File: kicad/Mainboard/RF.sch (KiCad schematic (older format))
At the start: 110 parts, among them J8 Antenna, Q3 BGA6589, T1 AFT05MS004NT1, U13 BGA2874, U5 ADF7021, U6 HMC546MS8GETR, U7 LM2904A, X1 12.288MHz

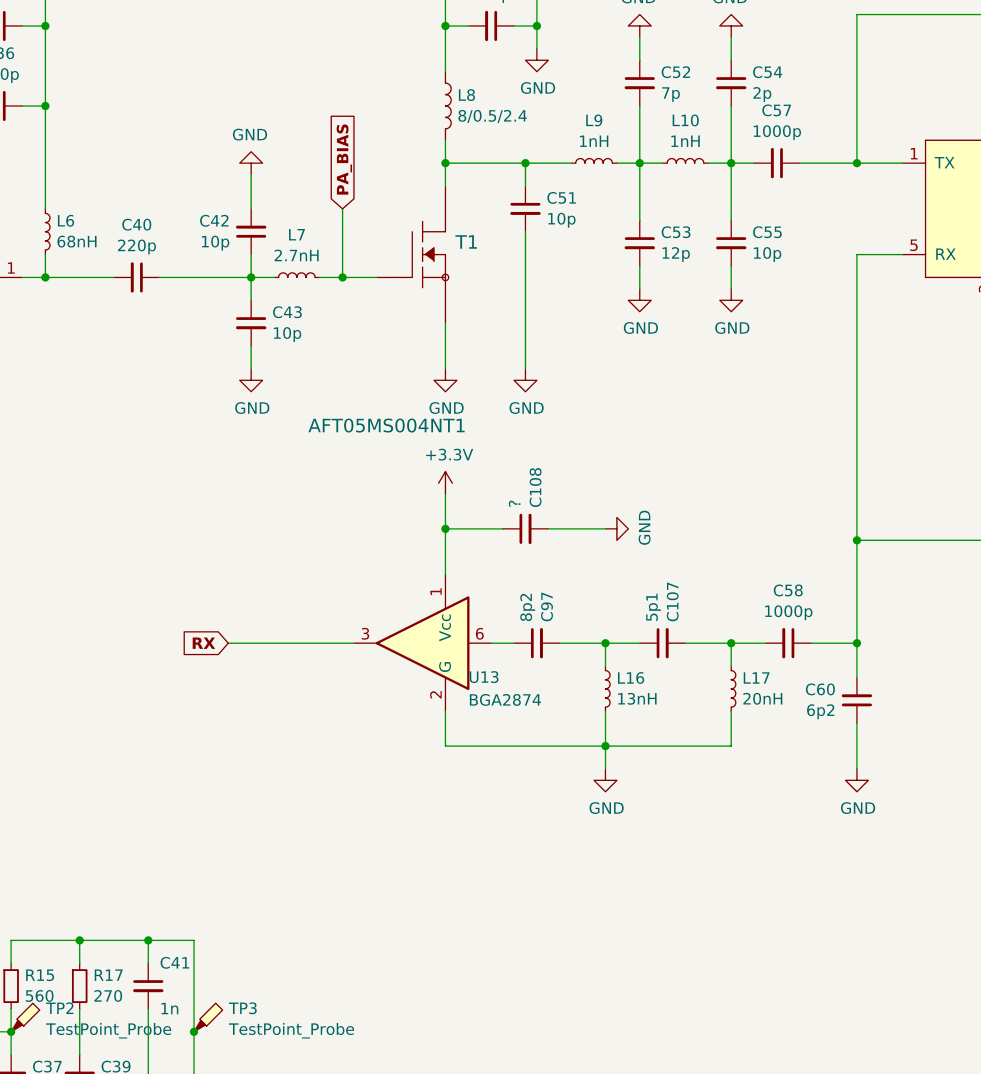
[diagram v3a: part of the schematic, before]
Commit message: added RF switch on-off transistor, plotted new schematic
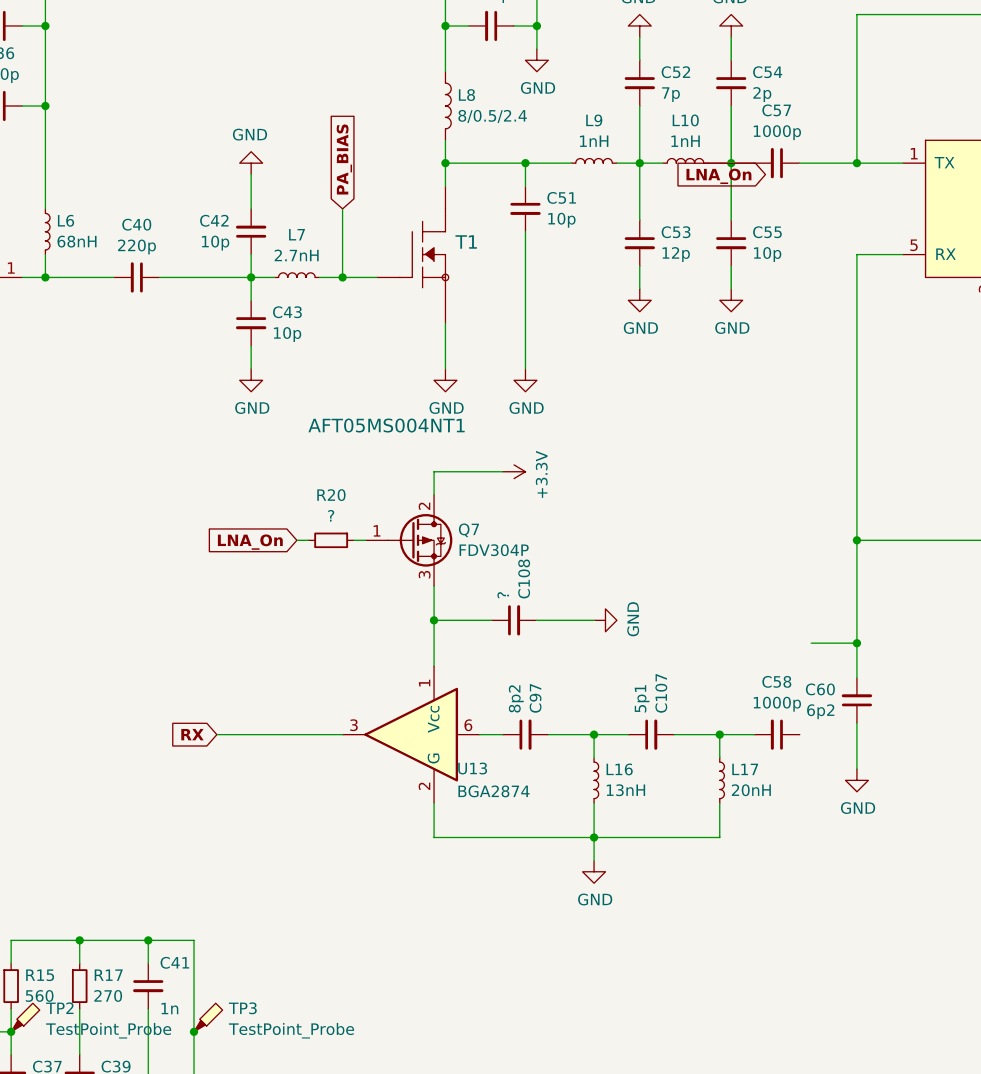
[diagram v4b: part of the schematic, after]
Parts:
- added Q7: FDV304P, Package_TO_SOT_SMD:SOT-23, symbol Device:Q_PMOS_GDS
- added R20: ?, Resistor_SMD:R_0603_1608Metric, symbol Mainboard-rescue:R_Small-Device
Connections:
- net +3V3: now also Q7.2 (D); no longer C108.1, U13.1 (Vcc)
- net at C60.2, L12.1, U6.5 (RX): no longer C58.1
- new net: C108.1, Q7.3 (S), U13.1 (Vcc)
- new net: Q7.1 (G), R20.1
- new net LNA_On: R20.2
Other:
- moved on the sheet: C107, C108, C58, C97, L16, L17, U13
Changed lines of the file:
@@
 L Mainboard-rescue:C_Small-device C58
 U 1 1 5DF79664
-P 7850 4600
-F 0 "C58" V 7621 4600 50  0000 C CNN
-F 1 "1000p" V 7712 4600 50  0000 C CNN
-F 2 "Capacitor_SMD:C_0603_1608Metric" H 7850 4600 50  0001 C CNN
-F 3 "~" H 7850 4600 50  0001 C CNN
-	1    7850 4600
+P 7800 5000
+F 0 "C58" V 7571 5000 50  0000 C CNN
+F 1 "1000p" V 7662 5000 50  0000 C CNN
+F 2 "Capacitor_SMD:C_0603_1608Metric" H 7800 5000 50  0001 C CNN
+F 3 "~" H 7800 5000 50  0001 C CNN
+	1    7800 5000
 	0    1    1    0
 $EndComp
@@
 Wire Wire Line
 	8150 2900 8150 4150
-Text GLabel 5400 4600 0    50   Input ~ 10
+Text GLabel 5350 5000 0    50   Input ~ 10
 RX
 Text GLabel 14950 4000 2    50   Input ~ 10
@@
 L RF_Amplifier:BGA2874 U13
 U 1 1 5EB02D36
-P 6250 4600
-F 0 "U13" H 6050 4450 50  0000 R CNN
-F 1 "BGA2874" H 6050 4350 50  0000 R CNN
-F 2 "Package_TO_SOT_SMD:SOT-363_SC-70-6" H 6200 3950 50  0001 C CNN
-F 3 "https://www.nxp.com/docs/en/data-sheet/BGA2874.pdf" H 6250 4600 50  0001 C CNN
-	1    6250 4600
+P 6200 5000
+F 0 "U13" H 6000 4850 50  0000 R CNN
+F 1 "BGA2874" H 6000 4750 50  0000 R CNN
+F 2 "Package_TO_SOT_SMD:SOT-363_SC-70-6" H 6150 4350 50  0001 C CNN
+F 3 "https://www.nxp.com/docs/en/data-sheet/BGA2874.pdf" H 6200 5000 50  0001 C CNN
+	1    6200 5000
 	-1   0    0    -1
 $EndComp
@@
 L Device:L_Small L17
 U 1 1 5EB6932C
-P 7600 4800
-F 0 "L17" H 7648 4846 50  0000 L CNN
-F 1 "20nH" H 7648 4755 50  0000 L CNN
-F 2 "Inductor_SMD:L_0603_1608Metric" H 7600 4800 50  0001 C CNN
-F 3 "~" H 7600 4800 50  0001 C CNN
-	1    7600 4800
+P 7550 5200
+F 0 "L17" H 7598 5246 50  0000 L CNN
+F 1 "20nH" H 7598 5155 50  0000 L CNN
+F 2 "Inductor_SMD:L_0603_1608Metric" H 7550 5200 50  0001 C CNN
+F 3 "~" H 7550 5200 50  0001 C CNN
+	1    7550 5200
 	1    0    0    -1
 $EndComp
@@
 L Mainboard-rescue:C_Small-Device C107
 U 1 1 5EB6AF5F
-P 7300 4600
-F 0 "C107" H 7208 4554 50  0000 R CNN
-F 1 "5p1" H 7208 4645 50  0000 R CNN
-F 2 "Capacitor_SMD:C_0603_1608Metric" H 7300 4600 50  0001 C CNN
-F 3 "~" H 7300 4600 50  0001 C CNN
-	1    7300 4600
+P 7250 5000
+F 0 "C107" H 7158 4954 50  0000 R CNN
+F 1 "5p1" H 7158 5045 50  0000 R CNN
+F 2 "Capacitor_SMD:C_0603_1608Metric" H 7250 5000 50  0001 C CNN
+F 3 "~" H 7250 5000 50  0001 C CNN
+	1    7250 5000
 	0    -1   1    0
 $EndComp
@@
 L Device:L_Small L16
 U 1 1 5EB6CEAB
-P 7050 4800
-F 0 "L16" H 7098 4846 50  0000 L CNN
-F 1 "13nH" H 7098 4755 50  0000 L CNN
-F 2 "Inductor_SMD:L_0603_1608Metric" H 7050 4800 50  0001 C CNN
-F 3 "~" H 7050 4800 50  0001 C CNN
-	1    7050 4800
+P 7000 5200
+F 0 "L16" H 7048 5246 50  0000 L CNN
+F 1 "13nH" H 7048 5155 50  0000 L CNN
+F 2 "Inductor_SMD:L_0603_1608Metric" H 7000 5200 50  0001 C CNN
+F 3 "~" H 7000 5200 50  0001 C CNN
+	1    7000 5200
 	1    0    0    -1
 $EndComp
@@
 L Mainboard-rescue:C_Small-Device C97
 U 1 1 5EB6D251
-P 6750 4600
-F 0 "C97" H 6658 4554 50  0000 R CNN
-F 1 "8p2" H 6658 4645 50  0000 R CNN
-F 2 "Capacitor_SMD:C_0603_1608Metric" H 6750 4600 50  0001 C CNN
-F 3 "~" H 6750 4600 50  0001 C CNN
-	1    6750 4600
+P 6700 5000
+F 0 "C97" H 6608 4954 50  0000 R CNN
+F 1 "8p2" H 6608 5045 50  0000 R CNN
+F 2 "Capacitor_SMD:C_0603_1608Metric" H 6700 5000 50  0001 C CNN
+F 3 "~" H 6700 5000 50  0001 C CNN
+	1    6700 5000
 	0    -1   1    0
 $EndComp
 Wire Wire Line
-	6550 4600 6650 4600
+	6500 5000 6600 5000
 $Comp
 L power:GND #PWR0120
 U 1 1 5EC16C67
-P 7050 5150
-F 0 "#PWR0120" H 7050 4900 50  0001 C CNN
-F 1 "GND" H 7055 4977 50  0000 C CNN
-F 2 "" H 7050 5150 50  0001 C CNN
-F 3 "" H 7050 5150 50  0001 C CNN
-	1    7050 5150
+P 7000 5550
+F 0 "#PWR0120" H 7000 5300 50  0001 C CNN
+F 1 "GND" H 7005 5377 50  0000 C CNN
+F 2 "" H 7000 5550 50  0001 C CNN
+F 3 "" H 7000 5550 50  0001 C CNN
+	1    7000 5550
 	1    0    0    -1
 $EndComp
@@
 L power:+3.3V #PWR0176
 U 1 1 5ECF6899
-P 6350 3950
-F 0 "#PWR0176" H 6350 3800 50  0001 C CNN
-F 1 "+3.3V" H 6365 4123 50  0000 C CNN
-F 2 "" H 6350 3950 50  0001 C CNN
-F 3 "" H 6350 3950 50  0001 C CNN
-	1    6350 3950
-	1    0    0    -1
+P 6600 3850
+F 0 "#PWR0176" H 6600 3700 50  0001 C CNN
+F 1 "+3.3V" H 6615 4023 50  0000 C CNN
+F 2 "" H 6600 3850 50  0001 C CNN
+F 3 "" H 6600 3850 50  0001 C CNN
+	1    6600 3850
+	0    1    1    0
 $EndComp
 $Comp
 L Mainboard-rescue:C_Small-Device C108
 U 1 1 5ED2084B
-P 6700 4100
-F 0 "C108" H 6608 4054 50  0000 R CNN
-F 1 "?" H 6608 4145 50  0000 R CNN
-F 2 "Capacitor_SMD:C_0603_1608Metric" H 6700 4100 50  0001 C CNN
-F 3 "~" H 6700 4100 50  0001 C CNN
-	1    6700 4100
+P 6650 4500
+F 0 "C108" H 6558 4454 50  0000 R CNN
+F 1 "?" H 6558 4545 50  0000 R CNN
+F 2 "Capacitor_SMD:C_0603_1608Metric" H 6650 4500 50  0001 C CNN
+F 3 "~" H 6650 4500 50  0001 C CNN
+	1    6650 4500
 	0    -1   1    0
 $EndComp
-Connection ~ 6350 4100
+Connection ~ 6300 4500
 $Comp
 L power:GND #PWR0177
 U 1 1 5ED3FE5B
-P 7050 4100
-F 0 "#PWR0177" H 7050 3850 50  0001 C CNN
-F 1 "GND" H 7055 3927 50  0000 C CNN
-F 2 "" H 7050 4100 50  0001 C CNN
-F 3 "" H 7050 4100 50  0001 C CNN
-	1    7050 4100
+P 7000 4500
+F 0 "#PWR0177" H 7000 4250 50  0001 C CNN
+F 1 "GND" H 7005 4327 50  0000 C CNN
+F 2 "" H 7000 4500 50  0001 C CNN
+F 3 "" H 7000 4500 50  0001 C CNN
+	1    7000 4500
 	0    -1   -1   0
 $EndComp
 Wire Wire Line
-	5400 4600 5950 4600
-Wire Wire Line
-	6800 4100 7050 4100
-Wire Wire Line
-	6350 4100 6600 4100
-Wire Wire Line
-	6350 3950 6350 4100
-Wire Wire Line
-	6350 4100 6350 4300
-Wire Wire Line
-	6850 4600 7050 4600
-Wire Wire Line
-	7050 4700 7050 4600
-Connection ~ 7050 4600
-Wire Wire Line
-	7050 4600 7200 4600
-Wire Wire Line
-	7400 4600 7600 4600
-Wire Wire Line
-	7600 4700 7600 4600
-Connection ~ 7600 4600
-Wire Wire Line
-	7600 4600 7750 4600
+	5350 5000 5900 5000
+Wire Wire Line
+	6750 4500 7000 4500
+Wire Wire Line
+	6300 4500 6550 4500
+Wire Wire Line
+	6300 4350 6300 4500
+Wire Wire Line
+	6300 4500 6300 4700
+Wire Wire Line
+	6800 5000 7000 5000
+Wire Wire Line
+	7000 5100 7000 5000
+Connection ~ 7000 5000
+Wire Wire Line
+	7000 5000 7150 5000
+Wire Wire Line
+	7350 5000 7550 5000
+Wire Wire Line
+	7550 5100 7550 5000
+Connection ~ 7550 5000
+Wire Wire Line
+	7550 5000 7700 5000
 Wire Wire Line
 	8150 4950 8150 5150
 Wire Wire Line
-	7600 4900 7600 5050
-Wire Wire Line
-	7600 5050 7050 5050
-Wire Wire Line
-	6350 5050 6350 4900
-Wire Wire Line
-	7050 4900 7050 5050
-Connection ~ 7050 5050
-Wire Wire Line
-	7050 5050 6350 5050
-Wire Wire Line
-	7050 5050 7050 5150
+	7550 5300 7550 5450
+Wire Wire Line
+	7550 5450 7000 5450
+Wire Wire Line
+	6300 5450 6300 5300
+Wire Wire Line
+	7000 5300 7000 5450
+Connection ~ 7000 5450
+Wire Wire Line
+	7000 5450 6300 5450
+Wire Wire Line
+	7000 5450 7000 5550
+Wire Wire Line
+	6300 3850 6300 3950
+Wire Wire Line
+	6300 3850 6600 3850
+$Comp
+L Mainboard-rescue:R_Small-Device R20
+U 1 1 5ECF3BC5
+P 5850 4150
+F 0 "R20" V 5654 4150 50  0000 C CNN
+F 1 "?" V 5745 4150 50  0000 C CNN
+F 2 "Resistor_SMD:R_0603_1608Metric" H 5850 4150 50  0001 C CNN
+F 3 "~" H 5850 4150 50  0001 C CNN
+	1    5850 4150
+	0    1    1    0
+$EndComp
+Wire Wire Line
+	5950 4150 6000 4150
+Wire Wire Line
+	5750 4150 5700 4150
+$Comp
+L Device:Q_PMOS_GDS Q7
+U 1 1 5ED3A378
+P 6200 4150
+F 0 "Q7" H 6405 4196 50  0000 L CNN
+F 1 "FDV304P" H 6405 4105 50  0000 L CNN
+F 2 "Package_TO_SOT_SMD:SOT-23" H 6400 4250 50  0001 C CNN
+F 3 "~" H 6200 4150 50  0001 C CNN
+	1    6200 4150
+	1    0    0    -1
+$EndComp
+Text GLabel 5700 4150 0    50   Input ~ 10
+LNA_On
+Text GLabel 7750 2550 0    50   Input ~ 10
+LNA_On
 $EndSCHEMATC

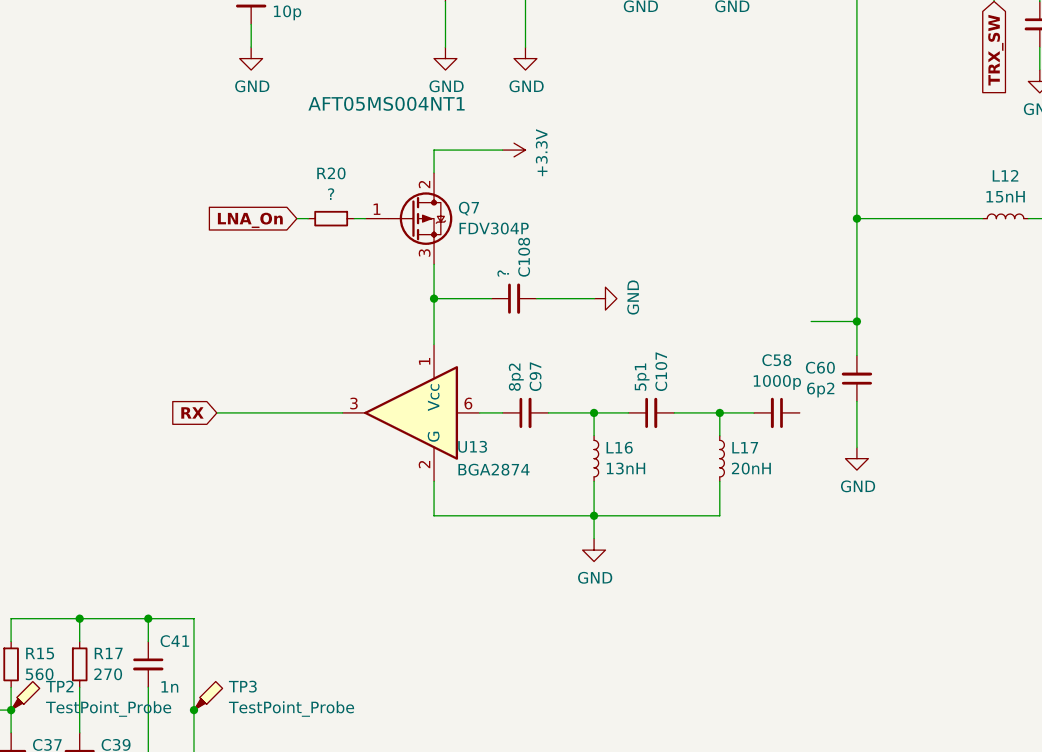
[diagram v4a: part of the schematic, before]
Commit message: fixed p-mos alignment :)
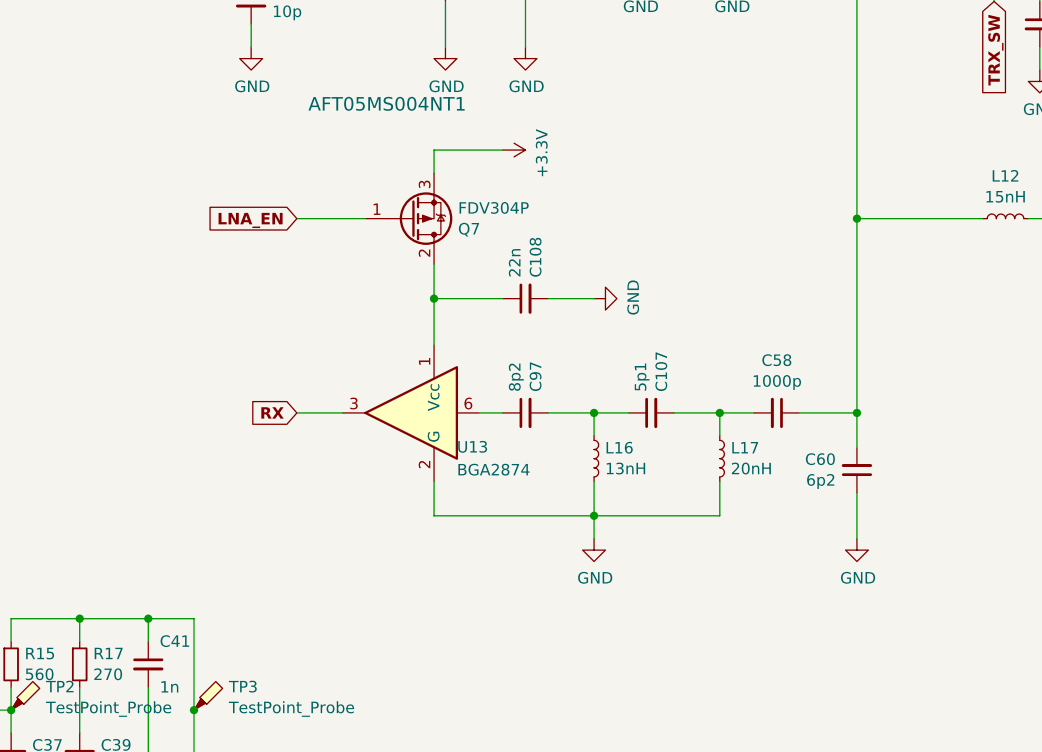
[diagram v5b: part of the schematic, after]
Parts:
- removed R20: ?, Resistor_SMD:R_0603_1608Metric, symbol Mainboard-rescue:R_Small-Device
- C108: value ? -> 22n
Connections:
- net +3V3: now also Q7.3 (S); no longer Q7.2 (D)
- net at C60.2, L12.1, U6.5 (RX): now also C58.1
- net at C108.1, U13.1 (Vcc): now also Q7.2 (D); no longer Q7.3 (S)
- net LNA_EN: now reaches Q7.1 (G)
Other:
- moved on the sheet: C108, C60
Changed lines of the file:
@@
 EESchema Schematic File Version 4
+LIBS:Mainboard-cache
 EELAYER 30 0
 EELAYER END
@@
 Wire Wire Line
 	8150 2900 8150 4150
-Text GLabel 5350 5000 0    50   Input ~ 10
+Text GLabel 5700 5000 0    50   Input ~ 10
 RX
 Text GLabel 14950 4000 2    50   Input ~ 10
@@
 	0    -1   -1   0
 $EndComp
-Connection ~ 8150 4150
 Wire Wire Line
 	9750 4150 9750 2700
@@
 L Mainboard-rescue:C_Small-Device C60
 U 1 1 5E09CAD6
-P 8150 4850
-F 0 "C60" H 8058 4804 50  0000 R CNN
-F 1 "6p2" H 8058 4895 50  0000 R CNN
-F 2 "Capacitor_SMD:C_0603_1608Metric" H 8150 4850 50  0001 C CNN
-F 3 "~" H 8150 4850 50  0001 C CNN
-	1    8150 4850
+P 8150 5250
+F 0 "C60" H 8058 5204 50  0000 R CNN
+F 1 "6p2" H 8058 5295 50  0000 R CNN
+F 2 "Capacitor_SMD:C_0603_1608Metric" H 8150 5250 50  0001 C CNN
+F 3 "~" H 8150 5250 50  0001 C CNN
+	1    8150 5250
 	1    0    0    1
 $EndComp
@@
 L power:GND #PWR098
 U 1 1 5E0A2231
-P 8150 5150
-F 0 "#PWR098" H 8150 4900 50  0001 C CNN
-F 1 "GND" H 8155 4977 50  0000 C CNN
-F 2 "" H 8150 5150 50  0001 C CNN
-F 3 "" H 8150 5150 50  0001 C CNN
-	1    8150 5150
-	1    0    0    -1
-$EndComp
-Wire Wire Line
-	8150 4150 8150 4600
+P 8150 5550
+F 0 "#PWR098" H 8150 5300 50  0001 C CNN
+F 1 "GND" H 8155 5377 50  0000 C CNN
+F 2 "" H 8150 5550 50  0001 C CNN
+F 3 "" H 8150 5550 50  0001 C CNN
+	1    8150 5550
+	1    0    0    -1
+$EndComp
 $Comp
 L Mainboard-rescue:C_Small-Device C62
@@
 	1    0    0    -1
 $EndComp
-Wire Wire Line
-	7950 4600 8150 4600
-Connection ~ 8150 4600
-Wire Wire Line
-	8150 4600 8150 4750
+Connection ~ 8150 5000
+Wire Wire Line
+	8150 5000 8150 5150
 $Comp
 L power:+3.3V #PWR0176
@@
 L Mainboard-rescue:C_Small-Device C108
 U 1 1 5ED2084B
-P 6650 4500
-F 0 "C108" H 6558 4454 50  0000 R CNN
-F 1 "?" H 6558 4545 50  0000 R CNN
-F 2 "Capacitor_SMD:C_0603_1608Metric" H 6650 4500 50  0001 C CNN
-F 3 "~" H 6650 4500 50  0001 C CNN
-	1    6650 4500
+P 6700 4500
+F 0 "C108" H 6608 4454 50  0000 R CNN
+F 1 "22n" H 6608 4545 50  0000 R CNN
+F 2 "Capacitor_SMD:C_0603_1608Metric" H 6700 4500 50  0001 C CNN
+F 3 "~" H 6700 4500 50  0001 C CNN
+	1    6700 4500
 	0    -1   1    0
 $EndComp
@@
 $EndComp
 Wire Wire Line
-	5350 5000 5900 5000
-Wire Wire Line
-	6750 4500 7000 4500
-Wire Wire Line
-	6300 4500 6550 4500
+	5700 5000 5900 5000
+Wire Wire Line
+	6800 4500 7000 4500
 Wire Wire Line
 	6300 4350 6300 4500
@@
 	7550 5000 7700 5000
 Wire Wire Line
-	8150 4950 8150 5150
+	8150 5350 8150 5550
 Wire Wire Line
 	7550 5300 7550 5450
@@
 Wire Wire Line
 	6300 3850 6600 3850
-$Comp
-L Mainboard-rescue:R_Small-Device R20
-U 1 1 5ECF3BC5
-P 5850 4150
-F 0 "R20" V 5654 4150 50  0000 C CNN
-F 1 "?" V 5745 4150 50  0000 C CNN
-F 2 "Resistor_SMD:R_0603_1608Metric" H 5850 4150 50  0001 C CNN
-F 3 "~" H 5850 4150 50  0001 C CNN
-	1    5850 4150
-	0    1    1    0
-$EndComp
-Wire Wire Line
-	5950 4150 6000 4150
-Wire Wire Line
-	5750 4150 5700 4150
 $Comp
 L Device:Q_PMOS_GDS Q7
@@
 F 3 "~" H 6200 4150 50  0001 C CNN
 	1    6200 4150
-	1    0    0    -1
+	1    0    0    1
 $EndComp
 Text GLabel 5700 4150 0    50   Input ~ 10
-LNA_On
+LNA_EN
 Text GLabel 7750 2550 0    50   Input ~ 10
 LNA_On
+Wire Wire Line
+	5700 4150 6000 4150
+Wire Wire Line
+	6300 4500 6600 4500
+Wire Wire Line
+	8150 4150 8150 5000
+Connection ~ 8150 4150
+Wire Wire Line
+	7900 5000 8150 5000
 $EndSCHEMATC
